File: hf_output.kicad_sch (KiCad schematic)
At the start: 9 parts, among them J31 MMCX_P, J32 MMCX_N

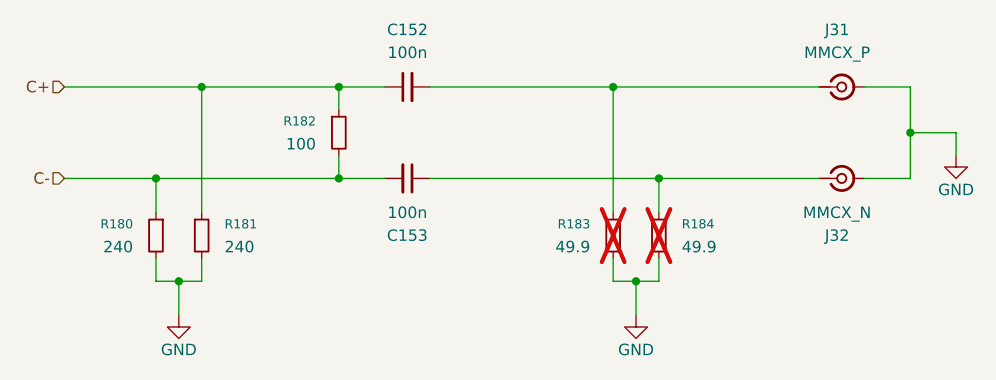
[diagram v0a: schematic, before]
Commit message: add NC and fix ERC
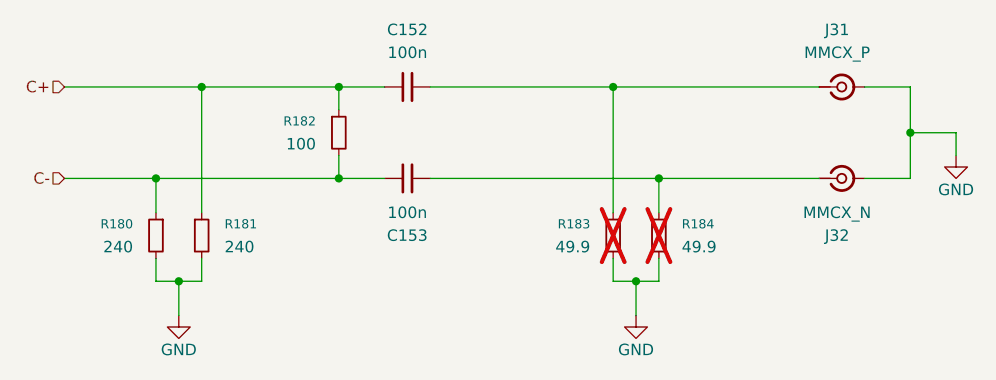
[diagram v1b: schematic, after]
